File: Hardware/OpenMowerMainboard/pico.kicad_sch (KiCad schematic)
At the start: 7 parts, among them U10 74HC4051, U11 Pico, U7 SN74LV1T34DBV, U9 74HC4051

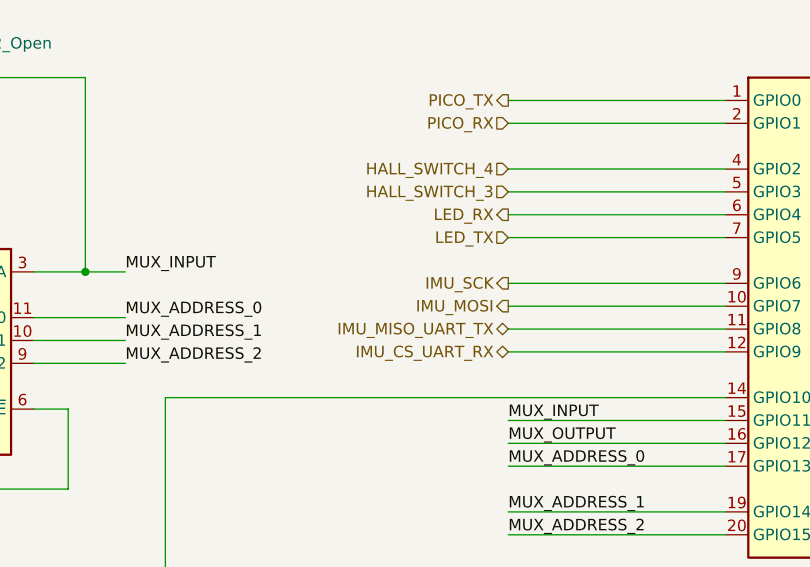
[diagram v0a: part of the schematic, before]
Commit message: fix(mb): swap pico GP4,5 with GP8,9
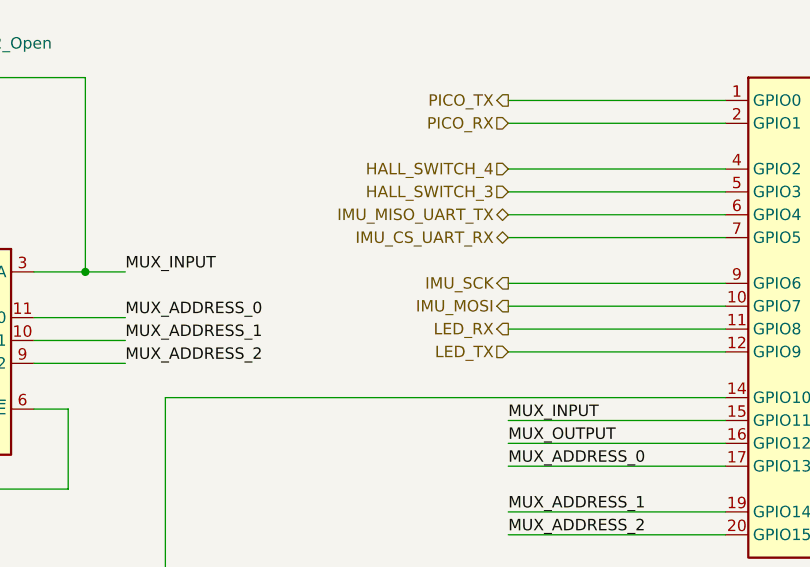
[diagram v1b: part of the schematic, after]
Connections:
- net IMU_CS_UART_RX: now also U11.7 (GPIO5); no longer U11.12 (GPIO9)
- net IMU_MISO_UART_TX: now also U11.6 (GPIO4); no longer U11.11 (GPIO8)
- net LED_RX: now also U11.11 (GPIO8); no longer U11.6 (GPIO4)
- net LED_TX: now also U11.12 (GPIO9); no longer U11.7 (GPIO5)
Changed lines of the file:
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@@
     (effects (font (size 1.27 1.27)) (justify left))
-  )
-  (hierarchical_label "LED_RX" (shape output) (at 173.99 80.01 180)
-    (effects (font (size 1.27 1.27)) (justify right))
   )
   (hierarchical_label "IMU_SCK" (shape output) (at 173.99 87.63 180)
@@
     (effects (font (size 1.27 1.27)) (justify right))
   )
-  (hierarchical_label "LED_TX" (shape input) (at 173.99 82.55 180)
-    (effects (font (size 1.27 1.27)) (justify right))
-  )
   (hierarchical_label "CURRENT_CHARGE" (shape input) (at 254 82.55 0)
     (effects (font (size 1.27 1.27)) (justify left))
   )
   (hierarchical_label "USS_1_ECHO" (shape input) (at 100.33 91.44 180)
+    (effects (font (size 1.27 1.27)) (justify right))
+  )
+  (hierarchical_label "LED_TX" (shape input) (at 173.99 95.25 180)
     (effects (font (size 1.27 1.27)) (justify right))
   )
@@
     (effects (font (size 1.27 1.27)) (justify right))
   )
-  (hierarchical_label "IMU_CS_UART_RX" (shape bidirectional) (at 173.99 95.25 180)
+  (hierarchical_label "IMU_MISO_UART_TX" (shape bidirectional) (at 173.99 80.01 180)
+    (effects (font (size 1.27 1.27)) (justify right))
+  )
+  (hierarchical_label "LED_RX" (shape output) (at 173.99 92.71 180)
+    (effects (font (size 1.27 1.27)) (justify right))
+  )
+  (hierarchical_label "IMU_CS_UART_RX" (shape bidirectional) (at 173.99 82.55 180)
     (effects (font (size 1.27 1.27)) (justify right))
   )
@@
     (effects (font (size 1.27 1.27)) (justify left))
   )
-  (hierarchical_label "IMU_MISO_UART_TX" (shape bidirectional) (at 173.99 92.71 180)
-    (effects (font (size 1.27 1.27)) (justify right))
-  )
   (hierarchical_label "HALL_SWITCH_3" (shape input) (at 173.99 77.47 180)

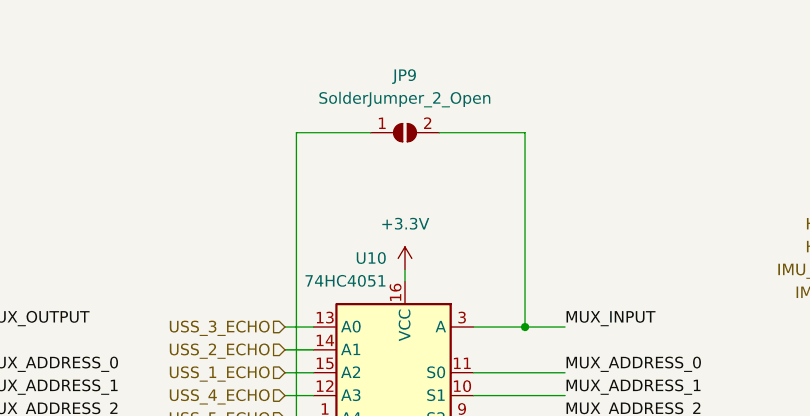
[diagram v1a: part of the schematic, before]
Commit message: feat: update to Kicad7, put back C2,C3
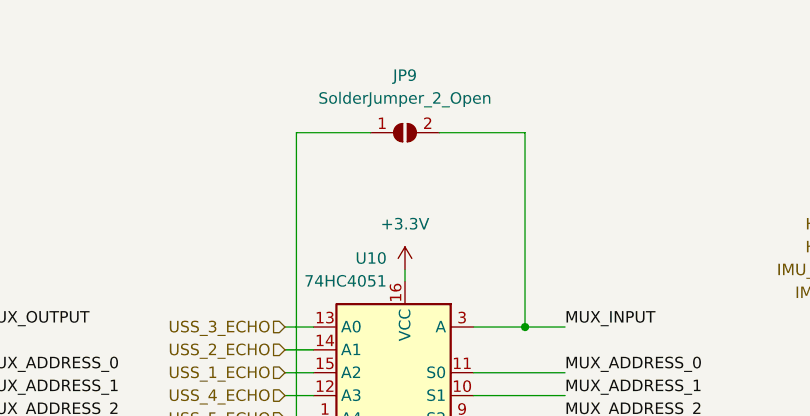
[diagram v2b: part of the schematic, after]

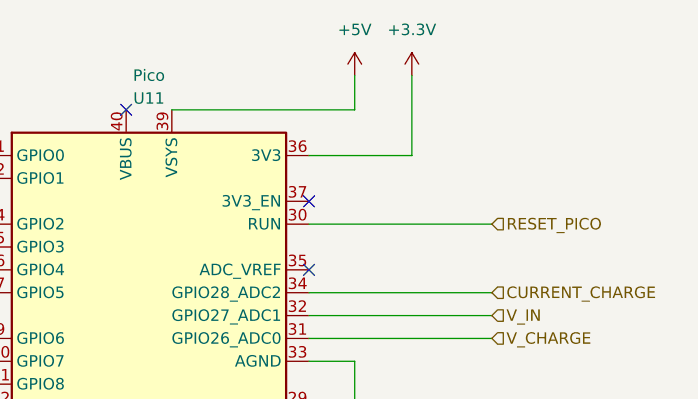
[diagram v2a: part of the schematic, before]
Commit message: feat: add F1 PPTC for 3.3V rail
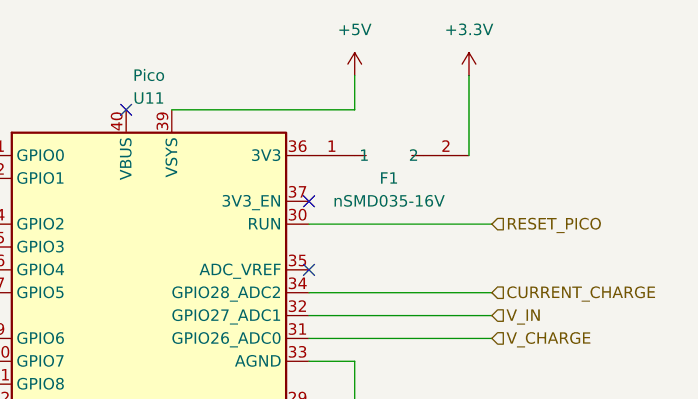
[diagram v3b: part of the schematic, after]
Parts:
- added F1: nSMD035-16V, lcsc:F1206, symbol lcsc:nSMD035-16V
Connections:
- net +3V3: now also F1.2; no longer U11.36 (3V3)
- new net: F1.1, U11.36 (3V3)
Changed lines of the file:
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@@
-    (stroke (width 0) (type default))
-  )
-  (wire (pts (xy 233.68 67.31) (xy 245.11 67.31))
     (stroke (width 0) (type default))
   )
@@
     (stroke (width 0) (type default))
   )
-  (wire (pts (xy 245.11 58.42) (xy 245.11 67.31))
-    (stroke (width 0) (type default))
-  )
   (wire (pts (xy 100.33 86.36) (xy 103.505 86.36))
     (stroke (width 0) (type default))
@@
   )
   (wire (pts (xy 160.655 170.815) (xy 173.99 170.815))
+    (stroke (width 0) (type default))
+  )
+  (wire (pts (xy 251.46 58.42) (xy 251.46 67.31))
     (stroke (width 0) (type default))
   )
@@
         (path "/c454102f-dc92-4550-9492-797fc8e6b49c/c4934db8-1638-4ac4-bd06-84d03b3fc106"
           (reference "U10") (unit 1)
+        )
+      )
+    )
+  )
+  (symbol (lib_id "lcsc:nSMD035-16V") (at 242.57 66.04 0) (unit 1)
+    (in_bom yes) (on_board yes) (dnp no) (fields_autoplaced)
+    (property "Reference" "F1" (at 242.57 69.85 0)
+      (effects (font (size 1.27 1.27)))
+    )
+    (property "Value" "nSMD035-16V" (at 242.57 72.39 0)
+      (effects (font (size 1.27 1.27)))
+    )
+    (property "Footprint" "lcsc:F1206" (at 242.57 74.93 0)
+      (effects (font (size 1.27 1.27)) hide)
+    )
+    (property "Datasheet" "https://lcsc.com/product-detail/Surface-Mount-Fuses_0-35A-16V-Self-healing-fuse_C70072.html" (at 242.57 77.47 0)
+      (effects (font (size 1.27 1.27)) hide)
+    )
+    (property "LCSC Part" "C70072" (at 242.57 80.01 0)
+      (effects (font (size 1.27 1.27)) hide)
+    )
+    (pin "1")
+    (pin "2")
+    (instances
+      (project "OpenMowerMainboard"
+        (path "/c454102f-dc92-4550-9492-797fc8e6b49c/c4934db8-1638-4ac4-bd06-84d03b3fc106"
+          (reference "F1") (unit 1)
         )
       )
@@
     )
   )
-  (symbol (lib_id "power:+3.3V") (at 245.11 58.42 0) (unit 1)
-    (in_bom yes) (on_board yes) (dnp no) (fields_autoplaced)
-    (property "Reference" "#PWR0144" (at 245.11 62.23 0)
-      (effects (font (size 1.27 1.27)) hide)
-    )
-    (property "Value" "+3.3V" (at 245.11 53.34 0)
-      (effects (font (size 1.27 1.27)))
-    )
-    (property "Footprint" "" (at 245.11 58.42 0)
-      (effects (font (size 1.27 1.27)) hide)
-    )
-    (property "Datasheet" "" (at 245.11 58.42 0)
-      (effects (font (size 1.27 1.27)) hide)
-    )
+  (symbol (lib_id "power:+3.3V") (at 251.46 58.42 0) (unit 1)
+    (in_bom yes) (on_board yes) (dnp no) (fields_autoplaced)
+    (property "Reference" "#PWR0144" (at 251.46 62.23 0)
+      (effects (font (size 1.27 1.27)) hide)
+    )
+    (property "Value" "+3.3V" (at 251.46 53.34 0)
+      (effects (font (size 1.27 1.27)))
+    )
+    (property "Footprint" "" (at 251.46 58.42 0)
+      (effects (font (size 1.27 1.27)) hide)
+    )
+    (property "Datasheet" "" (at 251.46 58.42 0)
+      (effects (font (size 1.27 1.27)) hide)
+    )
